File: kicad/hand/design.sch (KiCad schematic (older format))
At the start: 52 parts, among them P1 CONN_11, P2 CONN_11, SW1 SW_00, SW10 SW_10, SW11 SW_21, SW12 SW_22, SW13 SW_23, SW14 SW_24, SW15 SW_20, SW16 SW_31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

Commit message: starting work on a separate thumb board
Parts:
- removed P1, P2: CONN_11, symbol CONN_11
- added P1, P2: CONN_12, symbol CONN_12
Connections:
- net labels added: C2
- wire segments 110 -> 108
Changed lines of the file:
@@
 Sheet 1 1
 Title ""
-Date "4 feb 2014"
+Date "6 feb 2014"
 Rev ""
 Comp ""
@@
 Wire Wire Line
 	4750 2300 4900 2300
-Connection ~ 5400 2300
-Connection ~ 4750 2300
 Connection ~ 4100 2300
 Wire Wire Line
@@
 Wire Wire Line
 	1300 4950 1600 4950
-Connection ~ 1500 4950
-Connection ~ 1500 5050
 Connection ~ 1500 4850
-Connection ~ 6450 4950
-Text GLabel 2750 2100 1    60   Input ~ 0
+Text GLabel 2900 2300 1    60   Input ~ 0
 C0
-Text GLabel 3450 2100 1    60   Input ~ 0
+Text GLabel 3600 2300 1    60   Input ~ 0
 C1
-Text GLabel 4750 2100 1    60   Input ~ 0
+Text GLabel 4900 2300 1    60   Input ~ 0
 C3
-Text GLabel 5400 2100 1    60   Input ~ 0
+Text GLabel 5550 2300 1    60   Input ~ 0
 C4
 Wire Wire Line
-	2900 2100 2750 2100
-Wire Wire Line
-	4750 2100 4900 2100
-Connection ~ 5400 2100
-Connection ~ 4750 2100
-Wire Wire Line
-	5400 2100 5550 2100
-Connection ~ 2900 2300
-Connection ~ 3600 2300
-Connection ~ 4900 2300
-Connection ~ 5550 2300
-Wire Wire Line
 	6050 3050 6050 4550
 Wire Wire Line
-	3600 2100 3450 2100
-Wire Wire Line
-	4900 2100 4900 6850
-Wire Wire Line
-	5550 2100 5550 6750
-Wire Wire Line
-	3600 2100 3600 7050
-Wire Wire Line
-	2900 2100 2900 7150
+	4900 2300 4900 6850
+Wire Wire Line
+	5550 2300 5550 6750
+Wire Wire Line
+	3600 2300 3600 7050
 Wire Wire Line
 	1500 5050 1300 5050
 Wire Wire Line
 	6450 5050 6650 5050
-Text GLabel 1300 5150 3    60   Input ~ 0
+Text GLabel 1300 5250 3    60   Input ~ 0
 GND
-Text GLabel 6650 5150 3    60   Input ~ 0
+Text GLabel 6650 5250 3    60   Input ~ 0
 GND
 $Comp
-L CONN_11 P2
-U 1 1 52F07F77
-P 7000 4650
-F 0 "P2" V 6950 4650 60  0000 C CNN
-F 1 "CONN_11" V 7050 4650 60  0000 C CNN
-F 2 "" H 7000 4650 60  0000 C CNN
-F 3 "" H 7000 4650 60  0000 C CNN
-	1    7000 4650
+L CONN_12 P1
+U 1 1 52F07127
+P 950 4700
+F 0 "P1" V 900 4700 60  0000 C CNN
+F 1 "CONN_12" V 1000 4700 60  0000 C CNN
+F 2 "" H 950 4700 60  0000 C CNN
+F 3 "" H 950 4700 60  0000 C CNN
+	1    950  4700
+	-1   0    0    1
+$EndComp
+$Comp
+L CONN_12 P2
+U 1 1 52F07118
+P 7000 4700
+F 0 "P2" V 6950 4700 60  0000 C CNN
+F 1 "CONN_12" V 7050 4700 60  0000 C CNN
+F 2 "" H 7000 4700 60  0000 C CNN
+F 3 "" H 7000 4700 60  0000 C CNN
+	1    7000 4700
 	1    0    0    1
 $EndComp
-$Comp
-L CONN_11 P1
-U 1 1 52F07F9F
-P 950 4650
-F 0 "P1" V 900 4650 60  0000 C CNN
-F 1 "CONN_11" V 1000 4650 60  0000 C CNN
-F 2 "" H 950 4650 60  0000 C CNN
-F 3 "" H 950 4650 60  0000 C CNN
-	1    950  4650
-	-1   0    0    1
-$EndComp
+Wire Wire Line
+	1300 5250 1300 5150
+Wire Wire Line
+	6650 5250 6650 5150
+Text GLabel 4250 2300 1    60   Input ~ 0
+C2
+Wire Wire Line
+	2900 2300 2900 7150
 $EndSCHEMATC

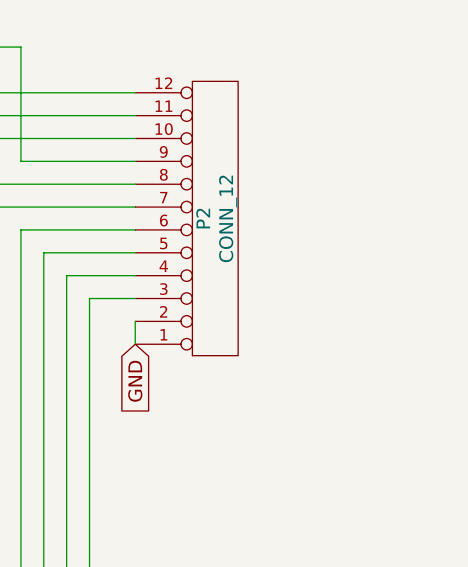
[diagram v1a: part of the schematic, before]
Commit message: adding mounting holes to gnd net
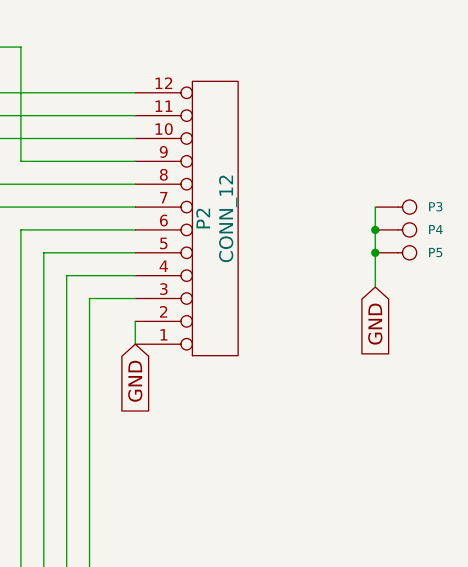
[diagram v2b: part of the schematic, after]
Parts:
- added P3, P4, P5: CONN_1, symbol CONN_1
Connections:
- net GND: now also P3.1, P4.1, P5.1
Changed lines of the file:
@@
 Wire Wire Line
 	2900 2300 2900 7150
+$Comp
+L CONN_1 P3
+U 1 1 52F400BD
+P 7850 4650
+F 0 "P3" H 7930 4650 40  0000 L CNN
+F 1 "CONN_1" H 7850 4705 30  0001 C CNN
+F 2 "" H 7850 4650 60  0000 C CNN
+F 3 "" H 7850 4650 60  0000 C CNN
+	1    7850 4650
+	1    0    0    -1
+$EndComp
+$Comp
+L CONN_1 P4
+U 1 1 52F400CA
+P 7850 4750
+F 0 "P4" H 7930 4750 40  0000 L CNN
+F 1 "CONN_1" H 7850 4805 30  0001 C CNN
+F 2 "" H 7850 4750 60  0000 C CNN
+F 3 "" H 7850 4750 60  0000 C CNN
+	1    7850 4750
+	1    0    0    -1
+$EndComp
+$Comp
+L CONN_1 P5
+U 1 1 52F400D0
+P 7850 4850
+F 0 "P5" H 7930 4850 40  0000 L CNN
+F 1 "CONN_1" H 7850 4905 30  0001 C CNN
+F 2 "" H 7850 4850 60  0000 C CNN
+F 3 "" H 7850 4850 60  0000 C CNN
+	1    7850 4850
+	1    0    0    -1
+$EndComp
+Text GLabel 7700 5000 3    60   Input ~ 0
+GND
+Wire Wire Line
+	7700 4650 7700 5000
+Connection ~ 7700 4850
+Connection ~ 7700 4750
 $EndSCHEMATC

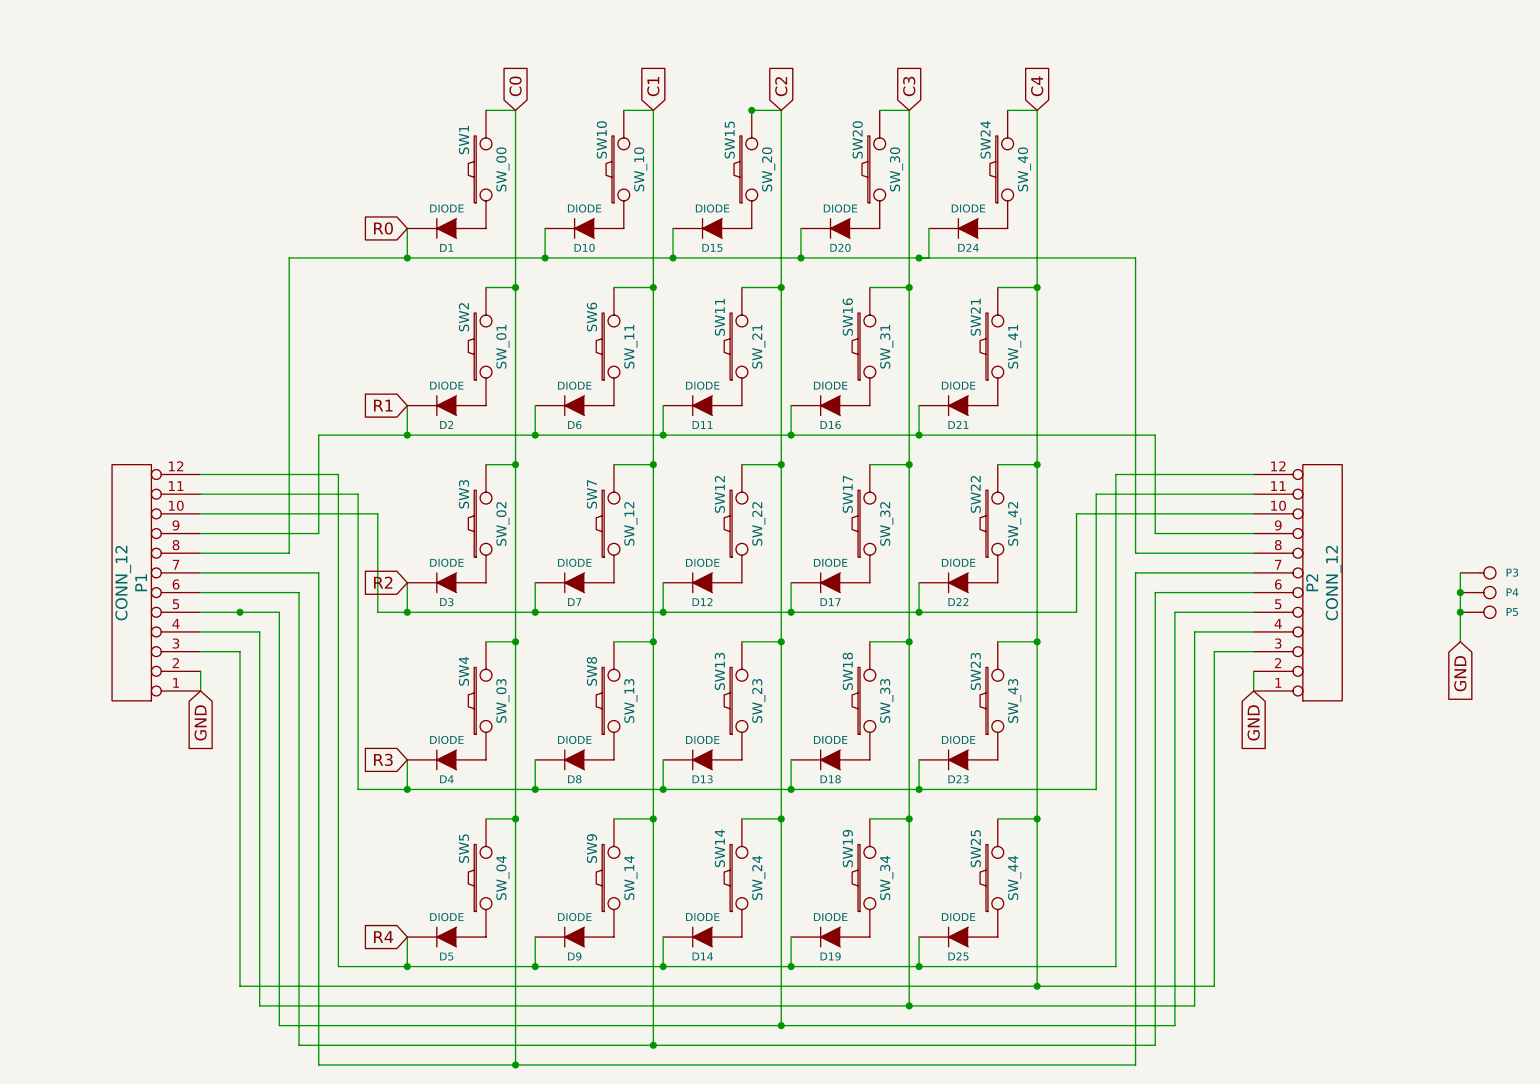
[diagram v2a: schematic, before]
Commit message: reversing all of the diodes
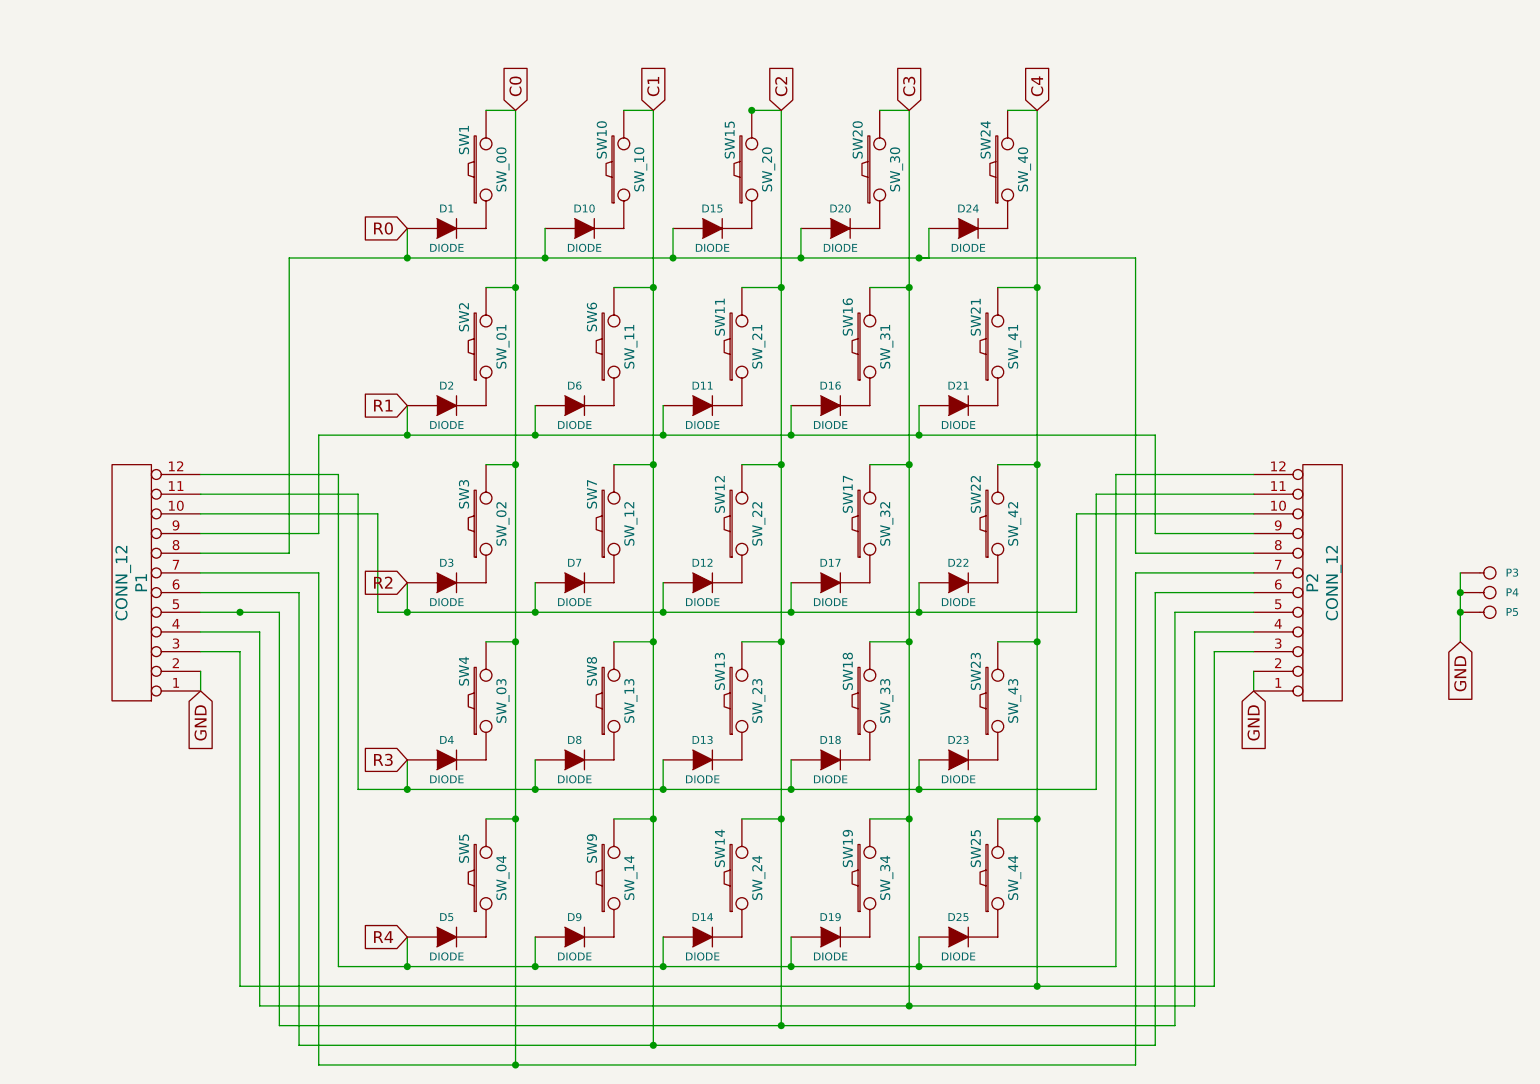
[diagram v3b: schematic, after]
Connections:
- net R0: now also D1.1 (A), D10.1 (A), D15.1 (A), D20.1 (A), D24.1 (A); no longer D1.2 (K), D10.2 (K), D15.2 (K), D20.2 (K), D24.2 (K)
- net R1: now also D11.1 (A), D16.1 (A), D2.1 (A), D21.1 (A), D6.1 (A); no longer D11.2 (K), D16.2 (K), D2.2 (K), D21.2 (K), D6.2 (K)
- net R2: now also D12.1 (A), D17.1 (A), D22.1 (A), D3.1 (A), D7.1 (A); no longer D12.2 (K), D17.2 (K), D22.2 (K), D3.2 (K), D7.2 (K)
- net R3: now also D13.1 (A), D18.1 (A), D23.1 (A), D4.1 (A), D8.1 (A); no longer D13.2 (K), D18.2 (K), D23.2 (K), D4.2 (K), D8.2 (K)
- net R4: now also D14.1 (A), D19.1 (A), D25.1 (A), D5.1 (A), D9.1 (A); no longer D14.2 (K), D19.2 (K), D25.2 (K), D5.2 (K), D9.2 (K)
- net at SW1.1: now also D1.2 (K); no longer D1.1 (A)
- net at SW10.1: now also D10.2 (K); no longer D10.1 (A)
- net at SW15.1: now also D15.2 (K); no longer D15.1 (A)
- net at SW20.1: now also D20.2 (K); no longer D20.1 (A)
- net at SW24.1: now also D24.2 (K); no longer D24.1 (A)
- net at SW2.1: now also D2.2 (K); no longer D2.1 (A)
- net at SW6.1: now also D6.2 (K); no longer D6.1 (A)
- net at SW11.1: now also D11.2 (K); no longer D11.1 (A)
- net at SW16.1: now also D16.2 (K); no longer D16.1 (A)
- net at SW21.1: now also D21.2 (K); no longer D21.1 (A)
- net at SW3.1: now also D3.2 (K); no longer D3.1 (A)
- net at SW7.1: now also D7.2 (K); no longer D7.1 (A)
- net at SW12.1: now also D12.2 (K); no longer D12.1 (A)
- net at SW17.1: now also D17.2 (K); no longer D17.1 (A)
- net at SW22.1: now also D22.2 (K); no longer D22.1 (A)
- net at SW4.1: now also D4.2 (K); no longer D4.1 (A)
- net at SW8.1: now also D8.2 (K); no longer D8.1 (A)
- net at SW13.1: now also D13.2 (K); no longer D13.1 (A)
- net at SW18.1: now also D18.2 (K); no longer D18.1 (A)
- net at SW23.1: now also D23.2 (K); no longer D23.1 (A)
- net at SW5.1: now also D5.2 (K); no longer D5.1 (A)
- net at SW9.1: now also D9.2 (K); no longer D9.1 (A)
- net at SW14.1: now also D14.2 (K); no longer D14.1 (A)
- net at SW19.1: now also D19.2 (K); no longer D19.1 (A)
- net at SW25.1: now also D25.2 (K); no longer D25.1 (A)
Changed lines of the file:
@@
 Sheet 1 1
 Title ""
-Date "6 feb 2014"
+Date "8 mar 2014"
 Rev ""
 Comp ""
@@
 F 3 "~" H 2550 2900 60  0000 C CNN
 	1    2550 2900
-	-1   0    0    1
+	1    0    0    -1
 $EndComp
 $Comp
@@
 F 3 "~" H 3250 2900 60  0000 C CNN
 	1    3250 2900
-	-1   0    0    1
+	1    0    0    -1
 $EndComp
 $Comp
@@
 F 3 "~" H 3900 2900 60  0000 C CNN
 	1    3900 2900
-	-1   0    0    1
+	1    0    0    -1
 $EndComp
 $Comp
@@
 F 3 "~" H 4550 2900 60  0000 C CNN
 	1    4550 2900
-	-1   0    0    1
+	1    0    0    -1
 $EndComp
 $Comp
@@
 F 3 "~" H 5200 2900 60  0000 C CNN
 	1    5200 2900
-	-1   0    0    1
+	1    0    0    -1
 $EndComp
 $Comp
@@
 F 3 "~" H 2550 3800 60  0000 C CNN
 	1    2550 3800
-	-1   0    0    1
+	1    0    0    -1
 $EndComp
 $Comp
@@
 F 3 "~" H 3200 3800 60  0000 C CNN
 	1    3200 3800
-	-1   0    0    1
+	1    0    0    -1
 $EndComp
 $Comp
@@
 F 3 "~" H 3850 3800 60  0000 C CNN
 	1    3850 3800
-	-1   0    0    1
+	1    0    0    -1
 $EndComp
 $Comp
@@
 F 3 "~" H 4500 3800 60  0000 C CNN
 	1    4500 3800
-	-1   0    0    1
+	1    0    0    -1
 $EndComp
 $Comp
@@
 F 3 "~" H 5150 3800 60  0000 C CNN
 	1    5150 3800
-	-1   0    0    1
+	1    0    0    -1
 $EndComp
 Text GLabel 2350 3800 0    60   Input ~ 0
@@
 F 3 "~" H 2550 4700 60  0000 C CNN
 	1    2550 4700
-	-1   0    0    1
+	1    0    0    -1
 $EndComp
 $Comp
@@
 F 3 "~" H 3200 4700 60  0000 C CNN
 	1    3200 4700
-	-1   0    0    1
+	1    0    0    -1
 $EndComp
 $Comp
@@
 F 3 "~" H 3850 4700 60  0000 C CNN
 	1    3850 4700
-	-1   0    0    1
+	1    0    0    -1
 $EndComp
 $Comp
@@
 F 3 "~" H 4500 4700 60  0000 C CNN
 	1    4500 4700
-	-1   0    0    1
+	1    0    0    -1
 $EndComp
 $Comp
@@
 F 3 "~" H 5150 4700 60  0000 C CNN
 	1    5150 4700
-	-1   0    0    1
+	1    0    0    -1
 $EndComp
 Text GLabel 2350 4700 0    60   Input ~ 0
@@
 F 3 "~" H 2550 5600 60  0000 C CNN
 	1    2550 5600
-	-1   0    0    1
+	1    0    0    -1
 $EndComp
 $Comp
@@
 F 3 "~" H 3200 5600 60  0000 C CNN
 	1    3200 5600
-	-1   0    0    1
+	1    0    0    -1
 $EndComp
 $Comp
@@
 F 3 "~" H 3850 5600 60  0000 C CNN
 	1    3850 5600
-	-1   0    0    1
+	1    0    0    -1
 $EndComp
 $Comp
@@
 F 3 "~" H 4500 5600 60  0000 C CNN
 	1    4500 5600
-	-1   0    0    1
+	1    0    0    -1
 $EndComp
 $Comp
@@
 F 3 "~" H 5150 5600 60  0000 C CNN
 	1    5150 5600
-	-1   0    0    1
+	1    0    0    -1
 $EndComp
 Text GLabel 2350 5600 0    60   Input ~ 0
@@
 F 3 "~" H 2550 6500 60  0000 C CNN
 	1    2550 6500
-	-1   0    0    1
+	1    0    0    -1
 $EndComp
 $Comp
@@
 F 3 "~" H 3200 6500 60  0000 C CNN
 	1    3200 6500
-	-1   0    0    1
+	1    0    0    -1
 $EndComp
 $Comp
@@
 F 3 "~" H 3850 6500 60  0000 C CNN
 	1    3850 6500
-	-1   0    0    1
+	1    0    0    -1
 $EndComp
 $Comp
@@
 F 3 "~" H 4500 6500 60  0000 C CNN
 	1    4500 6500
-	-1   0    0    1
+	1    0    0    -1
 $EndComp
 Text GLabel 2350 6500 0    60   Input ~ 0
@@
 F 3 "~" H 5150 6500 60  0000 C CNN
 	1    5150 6500
-	-1   0    0    1
+	1    0    0    -1
 $EndComp
 Wire Wire Line
